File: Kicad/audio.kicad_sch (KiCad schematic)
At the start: 70 parts, among them J201 CD Audio In, J202 AC'97 Audio Header, J203 Line Out, U201 TLV320AIC23BPW, U202 STX-4335-5BGP-S1, Y201 12M 20pF

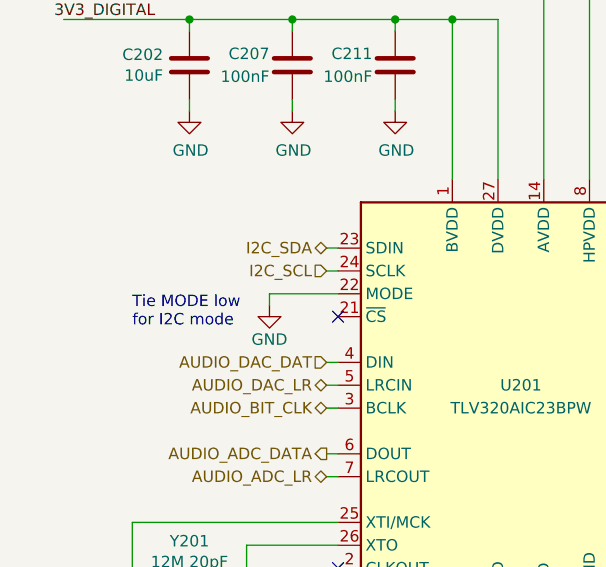
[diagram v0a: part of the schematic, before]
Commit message: Tie CS pin low on CODEC.
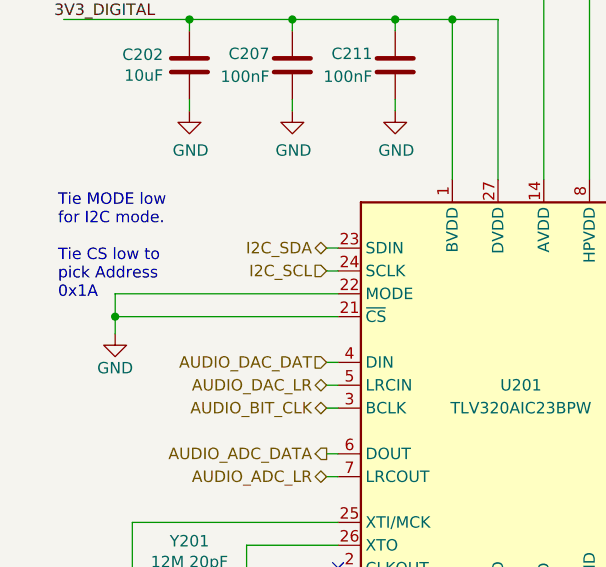
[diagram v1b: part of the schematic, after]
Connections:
- net GND: now also U201.21 (~{CS})
- no-connect marks 5 -> 4
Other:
- note added: "Tie MODE low for I2C mode. Tie CS low to pick Address 0x1A"
- note removed: "Tie MODE low for I2C mode"
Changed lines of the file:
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@@
   (junction (at 160.02 91.44) (diameter 0) (color 0 0 0 0)
   )
+  (junction (at 23.495 78.74) (diameter 0) (color 0 0 0 0)
+  )
   (junction (at 165.1 35.56) (diameter 0) (color 0 0 0 0)
   )
@@
   (junction (at 31.75 45.72) (diameter 0) (color 0 0 0 0)
   )
-  (no_connect (at 48.26 78.74))
   (no_connect (at 264.16 49.53))
   (no_connect (at 241.3 107.95))
@@
     (stroke (width 0) (type default) (color 0 0 0 0))
   )
-  (wire (pts (xy 48.26 76.2) (xy 40.64 76.2))
-    (stroke (width 0) (type default) (color 0 0 0 0))
-  )
   (wire (pts (xy 66.04 45.72) (xy 66.04 63.5))
     (stroke (width 0) (type default) (color 0 0 0 0))
@@
     (stroke (width 0) (type default) (color 0 0 0 0))
   )
+  (wire (pts (xy 23.495 78.74) (xy 48.26 78.74))
+    (stroke (width 0) (type default) (color 0 0 0 0))
+  )
   (wire (pts (xy 88.9 154.94) (xy 92.71 154.94))
     (stroke (width 0) (type default) (color 0 0 0 0))
@@
     (stroke (width 0) (type default) (color 0 0 0 0))
   )
+  (wire (pts (xy 23.495 78.74) (xy 23.495 80.645))
+    (stroke (width 0) (type default) (color 0 0 0 0))
+  )
   (wire (pts (xy 156.21 69.85) (xy 156.21 62.23))
     (stroke (width 0) (type default) (color 0 0 0 0))
@@
     (stroke (width 0) (type default) (color 0 0 0 0))
   )
-  (wire (pts (xy 40.64 76.2) (xy 40.64 77.47))
+  (wire (pts (xy 23.495 76.2) (xy 23.495 78.74))
     (stroke (width 0) (type default) (color 0 0 0 0))
   )
@@
   )
   (wire (pts (xy 113.03 99.06) (xy 113.03 123.19))
+    (stroke (width 0) (type default) (color 0 0 0 0))
+  )
+  (wire (pts (xy 23.495 76.2) (xy 48.26 76.2))
     (stroke (width 0) (type default) (color 0 0 0 0))
   )
@@
     (effects (font (size 2.54 2.54) (thickness 0.508) bold) (justify left bottom))
   )
-  (text "Tie MODE low\nfor I2C mode" (at 25.4 80.01 0)
+  (text "Tie MODE low\nfor I2C mode.\n\nTie CS low to\npick Address\n0x1A"
+    (at 17.145 76.835 0)
     (effects (font (size 1.27 1.27)) (justify left bottom))
   )
@@
     (pin "1")
   )
-  (symbol (lib_id "power:GND") (at 40.64 77.47 0) (unit 1)
-    (in_bom yes) (on_board yes)
-    (property "Reference" "#PWR0208" (id 0) (at 40.64 83.82 0)
-      (effects (font (size 1.27 1.27)) hide)
-    )
-    (property "Value" "GND" (id 1) (at 40.64 81.28 0))
-    (property "Footprint" "" (id 2) (at 40.64 77.47 0)
-      (effects (font (size 1.27 1.27)) hide)
-    )
-    (property "Datasheet" "" (id 3) (at 40.64 77.47 0)
-      (effects (font (size 1.27 1.27)) hide)
-    )
+  (symbol (lib_id "power:GND") (at 23.495 80.645 0) (unit 1)
+    (in_bom yes) (on_board yes)
+    (property "Reference" "#PWR0208" (id 0) (at 23.495 86.995 0)
+      (effects (font (size 1.27 1.27)) hide)
+    )
+    (property "Value" "GND" (id 1) (at 23.495 84.455 0))
+    (property "Footprint" "" (id 2) (at 23.495 80.645 0)
+      (effects (font (size 1.27 1.27)) hide)
+    )
+    (property "Datasheet" "" (id 3) (at 23.495 80.645 0)
+      (effects (font (size 1.27 1.27)) hide)
+    )

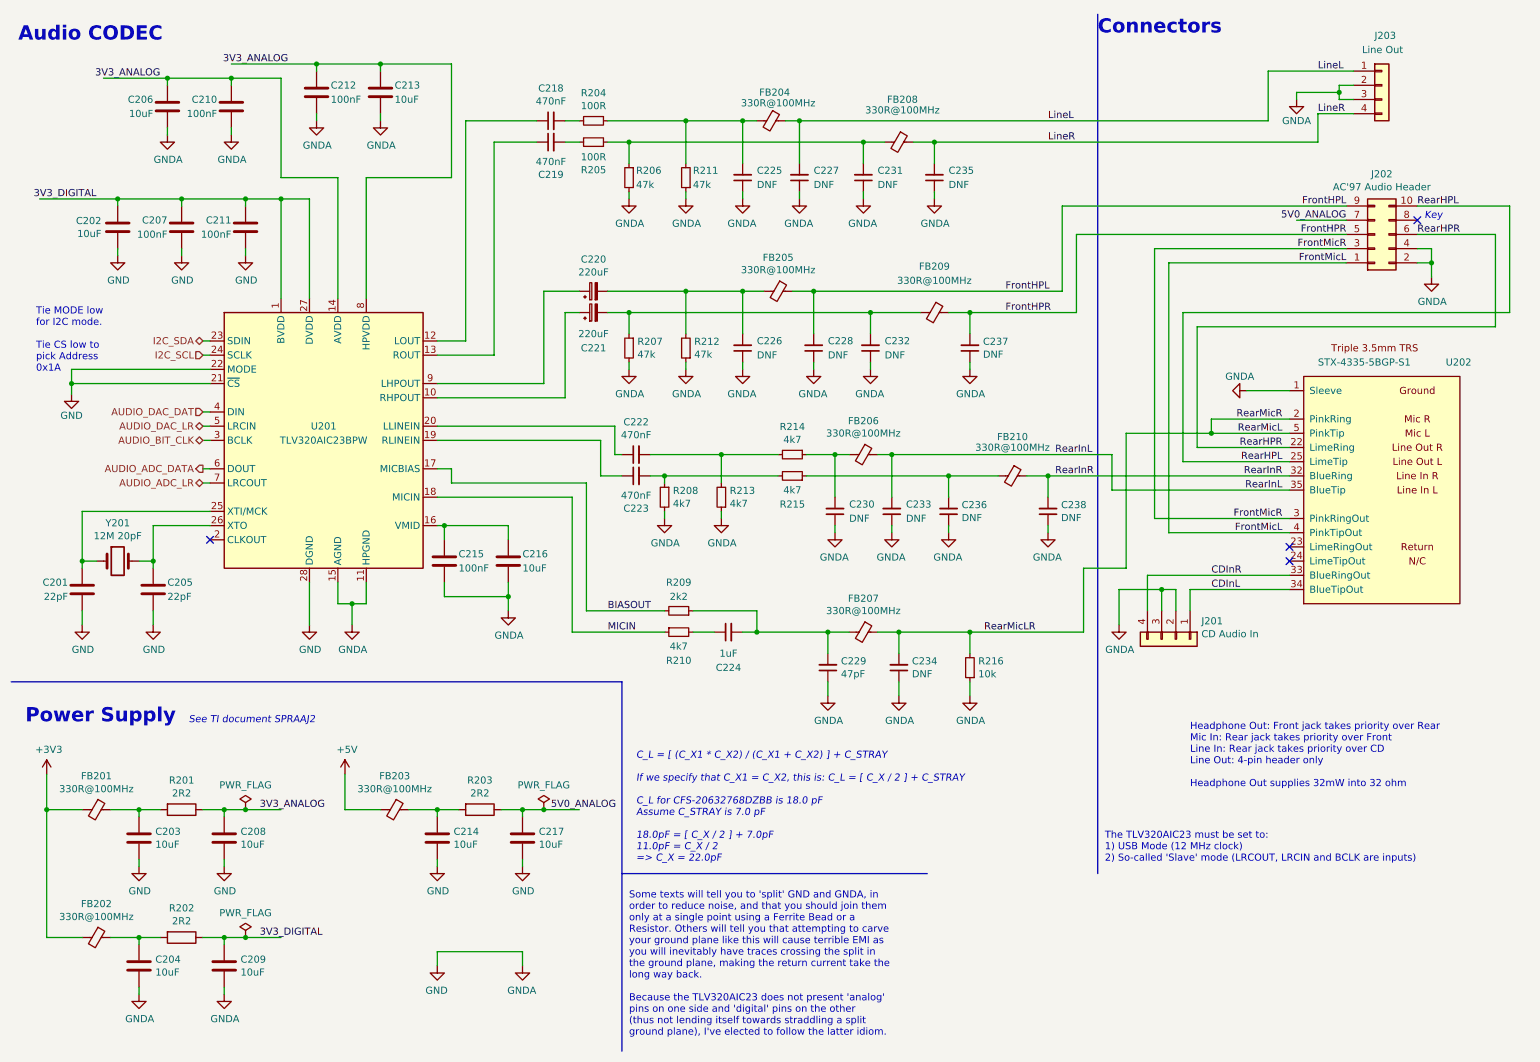
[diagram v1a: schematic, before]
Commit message: Retitle sheets and renumber parts.
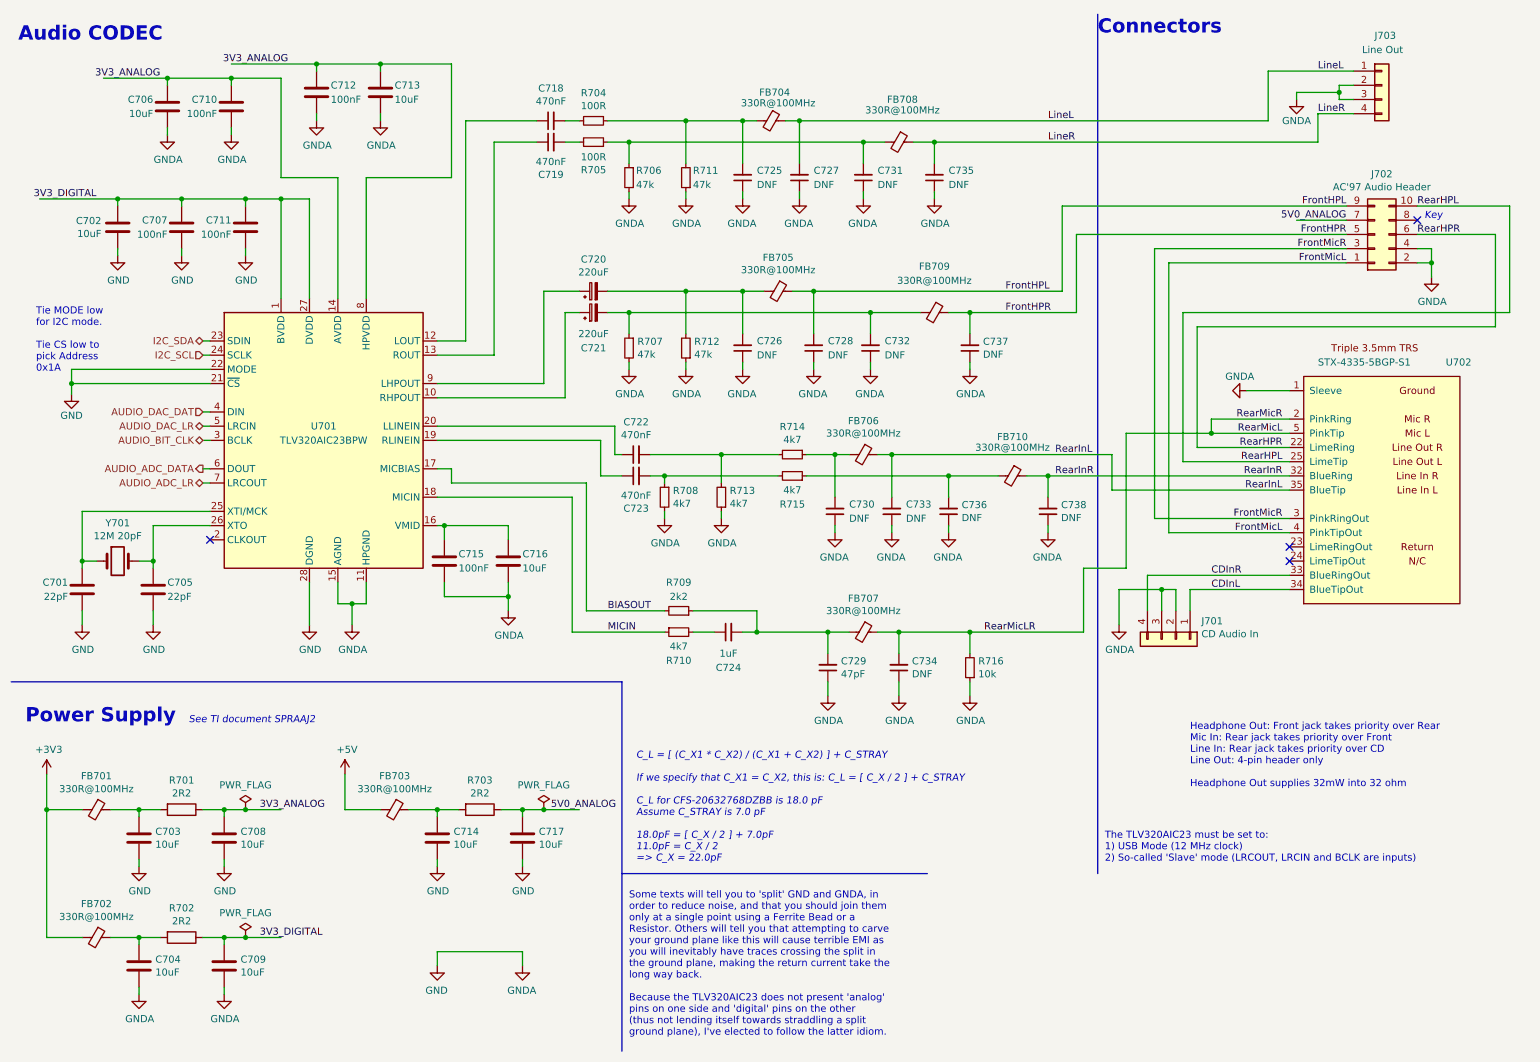
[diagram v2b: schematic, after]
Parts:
- renumbered C201 to C701, C202 to C702, C203 to C703, C204 to C704, C205 to C705, C206 to C706, C207 to C707, C208 to C708, C209 to C709, C210 to C710, C211 to C711, C212 to C712, C213 to C713, C214 to C714, C215 to C715, C216 to C716, C217 to C717, C218 to C718, C219 to C719, C220 to C720, C221 to C721, C222 to C722, C223 to C723, C224 to C724, C225 to C725, C226 to C726, C227 to C727, C228 to C728, C229 to C729, C230 to C730, C231 to C731, C232 to C732, C233 to C733, C234 to C734, C235 to C735, C236 to C736, C237 to C737, C238 to C738, FB201 to FB701, FB202 to FB702, FB203 to FB703, FB204 to FB704, FB205 to FB705, FB206 to FB706, FB207 to FB707, FB208 to FB708, FB209 to FB709, FB210 to FB710, J201 to J701, J202 to J702, J203 to J703, R201 to R701, R202 to R702, R203 to R703, R204 to R704, R205 to R705, R206 to R706, R207 to R707, R208 to R708, R209 to R709, R210 to R710, R211 to R711, R212 to R712, R213 to R713, R214 to R714, R215 to R715, R216 to R716, U201 to U701, U202 to U702, Y201 to Y701
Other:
- company: https://neotron-compute.github.io/ -> https://neotron-compute.github.io

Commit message: Set DAC to 1k/2k. Closes #77 Replaced some CPL resistors. Partial fix for #83 Added bridges for VGA I2C if ESD chip not fitted. Closes #51
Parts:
- R701, R702, R703: Digikey RMCF0805FT2R20-ND -> RMCF0805FT2R20CT-ND
- R704, R705: Digikey (none) -> RMCF0805FT100RCT-ND; MPN CPL-RES-0805-100-0.125W -> RMCF0805FT100R; Manufacturer CPL -> Stackpole
- R706, R707, R711, R712: Digikey RMCF0805FT47K5-ND -> RMCF0805FT47K5CT-ND
- R708, R710, R713, R714, R715: Digikey (none) -> RMCF0805FT4K70CT-ND; MPN CPL-RES-0805-4.7K-0.125W -> RMCF0805FT4K70; Manufacturer CPL -> Stackpole
- R709: Digikey RMCF0805FT2K20-ND -> RMCF0805FT2K20CT-ND
- R716: Digikey (none) -> RMCF0805FT10K0CT-ND; MPN CPL-RES-0805-10K-0.125W -> RMCF0805FT10K0; Manufacturer CPL -> Stackpole
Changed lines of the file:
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@@
       (effects (font (size 1.27 1.27)) hide)
     )
-    (property "Digikey" "~" (id 5) (at 116.84 31.75 0)
-      (effects (font (size 1.27 1.27)) hide)
-    )
-    (property "MPN" "CPL-RES-0805-100-0.125W" (id 6) (at 116.84 31.75 0)
-      (effects (font (size 1.27 1.27)) hide)
-    )
-    (property "Manufacturer" "CPL" (id 7) (at 116.84 31.75 0)
+    (property "Digikey" "RMCF0805FT100RCT-ND" (id 5) (at 116.84 31.75 0)
+      (effects (font (size 1.27 1.27)) hide)
+    )
+    (property "MPN" "RMCF0805FT100R" (id 6) (at 116.84 31.75 0)
+      (effects (font (size 1.27 1.27)) hide)
+    )
+    (property "Manufacturer" "Stackpole" (id 7) (at 116.84 31.75 0)
       (effects (font (size 1.27 1.27)) hide)
     )
@@
       (effects (font (size 1.27 1.27)) hide)
     )
-    (property "Digikey" "~" (id 5) (at 116.84 35.56 0)
-      (effects (font (size 1.27 1.27)) hide)
-    )
-    (property "MPN" "CPL-RES-0805-100-0.125W" (id 6) (at 116.84 35.56 0)
-      (effects (font (size 1.27 1.27)) hide)
-    )
-    (property "Manufacturer" "CPL" (id 7) (at 116.84 35.56 0)
+    (property "Digikey" "RMCF0805FT100RCT-ND" (id 5) (at 116.84 35.56 0)
+      (effects (font (size 1.27 1.27)) hide)
+    )
+    (property "MPN" "RMCF0805FT100R" (id 6) (at 116.84 35.56 0)
+      (effects (font (size 1.27 1.27)) hide)
+    )
+    (property "Manufacturer" "Stackpole" (id 7) (at 116.84 35.56 0)
       (effects (font (size 1.27 1.27)) hide)
     )
@@
       (effects (font (size 1.27 1.27)) hide)
     )
-    (property "Digikey" "RMCF0805FT47K5-ND" (id 5) (at 123.19 41.91 0)
+    (property "Digikey" "RMCF0805FT47K5CT-ND" (id 5) (at 123.19 41.91 0)
       (effects (font (size 1.27 1.27)) hide)
     )
@@
       (effects (font (size 1.27 1.27)) hide)
     )
-    (property "Digikey" "RMCF0805FT47K5-ND" (id 5) (at 133.35 41.91 0)
+    (property "Digikey" "RMCF0805FT47K5CT-ND" (id 5) (at 133.35 41.91 0)
       (effects (font (size 1.27 1.27)) hide)
     )
@@
       (effects (font (size 1.27 1.27)) hide)
     )
-    (property "Digikey" "RMCF0805FT47K5-ND" (id 5) (at 123.19 72.39 0)
+    (property "Digikey" "RMCF0805FT47K5CT-ND" (id 5) (at 123.19 72.39 0)
       (effects (font (size 1.27 1.27)) hide)
     )
@@
       (effects (font (size 1.27 1.27)) hide)
     )
-    (property "Digikey" "RMCF0805FT47K5-ND" (id 5) (at 133.35 72.39 0)
+    (property "Digikey" "RMCF0805FT47K5CT-ND" (id 5) (at 133.35 72.39 0)
       (effects (font (size 1.27 1.27)) hide)
     )
@@
       (effects (font (size 1.27 1.27)) hide)
     )
-    (property "Digikey" "RMCF0805FT2R20-ND" (id 5) (at 43.18 154.94 0)
+    (property "Digikey" "RMCF0805FT2R20CT-ND" (id 5) (at 43.18 154.94 0)
       (effects (font (size 1.27 1.27)) hide)
     )
@@
       (effects (font (size 1.27 1.27)) hide)
     )
-    (property "Digikey" "RMCF0805FT2R20-ND" (id 5) (at 43.18 177.8 0)
+    (property "Digikey" "RMCF0805FT2R20CT-ND" (id 5) (at 43.18 177.8 0)
       (effects (font (size 1.27 1.27)) hide)
     )
@@
       (effects (font (size 1.27 1.27)) hide)
     )
-    (property "Digikey" "~" (id 5) (at 152.4 91.44 0)
-      (effects (font (size 1.27 1.27)) hide)
-    )
-    (property "MPN" "CPL-RES-0805-4.7K-0.125W" (id 6) (at 152.4 91.44 0)
-      (effects (font (size 1.27 1.27)) hide)
-    )
-    (property "Manufacturer" "CPL" (id 7) (at 152.4 91.44 0)
+    (property "Digikey" "RMCF0805FT4K70CT-ND" (id 5) (at 152.4 91.44 0)
+      (effects (font (size 1.27 1.27)) hide)
+    )
+    (property "MPN" "RMCF0805FT4K70" (id 6) (at 152.4 91.44 0)
+      (effects (font (size 1.27 1.27)) hide)
+    )
+    (property "Manufacturer" "Stackpole" (id 7) (at 152.4 91.44 0)
       (effects (font (size 1.27 1.27)) hide)
     )
@@
       (effects (font (size 1.27 1.27)) hide)
     )
-    (property "Digikey" "~" (id 5) (at 152.4 95.25 0)
-      (effects (font (size 1.27 1.27)) hide)
-    )
-    (property "MPN" "CPL-RES-0805-4.7K-0.125W" (id 6) (at 152.4 95.25 0)
-      (effects (font (size 1.27 1.27)) hide)
-    )
-    (property "Manufacturer" "CPL" (id 7) (at 152.4 95.25 0)
+    (property "Digikey" "RMCF0805FT4K70CT-ND" (id 5) (at 152.4 95.25 0)
+      (effects (font (size 1.27 1.27)) hide)
+    )
+    (property "MPN" "RMCF0805FT4K70" (id 6) (at 152.4 95.25 0)
+      (effects (font (size 1.27 1.27)) hide)
+    )
+    (property "Manufacturer" "Stackpole" (id 7) (at 152.4 95.25 0)
       (effects (font (size 1.27 1.27)) hide)
     )
@@
       (effects (font (size 1.27 1.27)) hide)
     )
-    (property "Digikey" "~" (id 5) (at 129.54 99.06 0)
-      (effects (font (size 1.27 1.27)) hide)
-    )
-    (property "MPN" "CPL-RES-0805-4.7K-0.125W" (id 6) (at 129.54 99.06 0)
-      (effects (font (size 1.27 1.27)) hide)
-    )
-    (property "Manufacturer" "CPL" (id 7) (at 129.54 99.06 0)
+    (property "Digikey" "RMCF0805FT4K70CT-ND" (id 5) (at 129.54 99.06 0)
+      (effects (font (size 1.27 1.27)) hide)
+    )
+    (property "MPN" "RMCF0805FT4K70" (id 6) (at 129.54 99.06 0)
+      (effects (font (size 1.27 1.27)) hide)
+    )
+    (property "Manufacturer" "Stackpole" (id 7) (at 129.54 99.06 0)
       (effects (font (size 1.27 1.27)) hide)
     )
@@
       (effects (font (size 1.27 1.27)) hide)
     )
-    (property "Digikey" "~" (id 5) (at 139.7 99.06 0)
-      (effects (font (size 1.27 1.27)) hide)
-    )
-    (property "MPN" "CPL-RES-0805-4.7K-0.125W" (id 6) (at 139.7 99.06 0)
-      (effects (font (size 1.27 1.27)) hide)
-    )
-    (property "Manufacturer" "CPL" (id 7) (at 139.7 99.06 0)
+    (property "Digikey" "RMCF0805FT4K70CT-ND" (id 5) (at 139.7 99.06 0)
+      (effects (font (size 1.27 1.27)) hide)
+    )
+    (property "MPN" "RMCF0805FT4K70" (id 6) (at 139.7 99.06 0)
+      (effects (font (size 1.27 1.27)) hide)
+    )
+    (property "Manufacturer" "Stackpole" (id 7) (at 139.7 99.06 0)
       (effects (font (size 1.27 1.27)) hide)
     )
@@
       (effects (font (size 1.27 1.27)) hide)
     )
-    (property "Digikey" "RMCF0805FT2R20-ND" (id 5) (at 96.52 154.94 0)
+    (property "Digikey" "RMCF0805FT2R20CT-ND" (id 5) (at 96.52 154.94 0)
       (effects (font (size 1.27 1.27)) hide)
     )
@@
       (effects (font (size 1.27 1.27)) hide)
     )
-    (property "Digikey" "~" (id 5) (at 132.08 123.19 0)
-      (effects (font (size 1.27 1.27)) hide)
-    )
-    (property "MPN" "CPL-RES-0805-4.7K-0.125W" (id 6) (at 132.08 123.19 0)
-      (effects (font (size 1.27 1.27)) hide)
-    )
-    (property "Manufacturer" "CPL" (id 7) (at 132.08 123.19 0)
+    (property "Digikey" "RMCF0805FT4K70CT-ND" (id 5) (at 132.08 123.19 0)
+      (effects (font (size 1.27 1.27)) hide)
+    )
+    (property "MPN" "RMCF0805FT4K70" (id 6) (at 132.08 123.19 0)
+      (effects (font (size 1.27 1.27)) hide)
+    )
+    (property "Manufacturer" "Stackpole" (id 7) (at 132.08 123.19 0)
       (effects (font (size 1.27 1.27)) hide)
     )
@@
       (effects (font (size 1.27 1.27)) hide)
     )
-    (property "Digikey" "RMCF0805FT2K20-ND" (id 5) (at 132.08 119.38 0)
+    (property "Digikey" "RMCF0805FT2K20CT-ND" (id 5) (at 132.08 119.38 0)
       (effects (font (size 1.27 1.27)) hide)
     )
@@
       (effects (font (size 1.27 1.27)) hide)
     )
-    (property "Digikey" "~" (id 5) (at 184.15 129.54 0)
-      (effects (font (size 1.27 1.27)) hide)
-    )
-    (property "MPN" "CPL-RES-0805-10K-0.125W" (id 6) (at 184.15 129.54 0)
-      (effects (font (size 1.27 1.27)) hide)
-    )
-    (property "Manufacturer" "CPL" (id 7) (at 184.15 129.54 0)
-      (effects (font (size 1.27 1.27)) hide)
-    )
+    (property "Digikey" "RMCF0805FT10K0CT-ND" (id 5) (at 184.15 129.54 0)
+      (effects (font (size 1.27 1.27)) hide)
+    )
+    (property "MPN" "RMCF0805FT10K0" (id 6) (at 184.15 129.54 0)
+      (effects (font (size 1.27 1.27)) hide)
+    )
+    (property "Manufacturer" "Stackpole" (id 7) (at 184.15 129.54 0)
+      (effects (font (size 1.27 1.27)) hide)
+    )

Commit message: Removed all CPL parts, and changed standby PSU.
The Holtek was a SOT-89 that had a completely different pinout to
every other SOT-89 3.3V LDO out there. To avoid confusion I
wanted to replace it, but the only other basic JLCPCB parts
were the AMS1117 (huge quiescent current) and something only
rated to 7V input voltage (this LDO gets the full VDC in).

So, I used a TO-92 footprint and picked an LP2950N.

This, however, needs some ESR on the output cap, so I made
that a 2.2uF electrolytic.

I also removed the 2x 10uF output caps on the K7805 and set
just one 22uF as specified in the datasheet.
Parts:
- C702, C703, C704, C706, C708, C709, C713, C714, C716, C717: Digikey (none) -> 490-3886-1-ND; MPN CPL-CAP-X5R-0805-10UF-16V -> GRM21BR61C106KE15L; Manufacturer CPL -> Murata; Mouser (none) -> 81-GRM21BR61C106KE15
- C707, C710, C711, C712, C715: Digikey (none) -> 399-C0805C104M5RAC7800CT-ND; MPN CPL-CAP-X7R-0805-100NF-50V -> C0805C104M5RACTU; Manufacturer CPL -> Kemet; Mouser (none) -> 80-C0805C104M5R
- C720, C721: Digikey (none) -> P5183-ND; MPN CPL-CAP-ALU-RAD-220UF-50V -> ECA-1HM221; Manufacturer CPL -> Panasonic; Mouser (none) -> 667-ECA-1HM221
- C724: Digikey (none) -> 311-1456-1-ND; MPN CPL-CAP-X7R-0805-1UF-25V -> CC0805KKX7R8BB105; Manufacturer CPL -> Yageo; Mouser (none) -> 603-CC805KKX7R8BB105
- FB701, FB702, FB703, FB704, FB705, FB706, FB707, FB708, FB709, FB710: Digikey (none) -> 490-5988-6-ND; MPN CPL-IND-FER-330OHM-1.5A -> BLM21PG331SN1D; Manufacturer CPL -> Murata; Mouser (none) -> 81-BLM21P331SG
- Y701: Digikey (none) -> 535-9116-1-ND; MPN CPL-OSC-CRY-12MHZ-18PF -> ABM3B-12.000MHZ-B2-T; Manufacturer CPL -> Abracon; Mouser (none) -> 815-ABM3B-12-B2
